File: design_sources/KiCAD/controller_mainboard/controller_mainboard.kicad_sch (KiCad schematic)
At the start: 34 parts, among them J1 XT-90, J10 01x08_2.54mm _socket, J11 2P_screw_term, J12 2P_screw_term, J13 2P_screw_term, J14 2P_screw_term, J2 XT-60, J24 XT-60, J25 XT-60, J3 USB_C_Receptacle_USB2.0_16P, J4 01x08_2.54mm _socket, J5 01x08_2.54mm _socket, J6 01x08_2.54mm _socket, J7 02x18_2.54mm_socket, J8 Conn_01x10_2.54mm_socket, J9 01x08_2.54mm _socket, Q1 2N7002, U12 USBLC6-4SC6

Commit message: Advanced the hardware layout further.
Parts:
- added H1, H2, H3, H4, H5, H6, H7, H8: MountingHole, MountingHole:MountingHole_3.2mm_M3_DIN965, symbol Mechanical:MountingHole
- J7: footprint Connector_PinHeader_2.54mm:PinHeader_2x18_P2.54mm_Vertical -> Connector_PinSocket_2.54mm:PinSocket_2x18_P2.54mm_Vertical

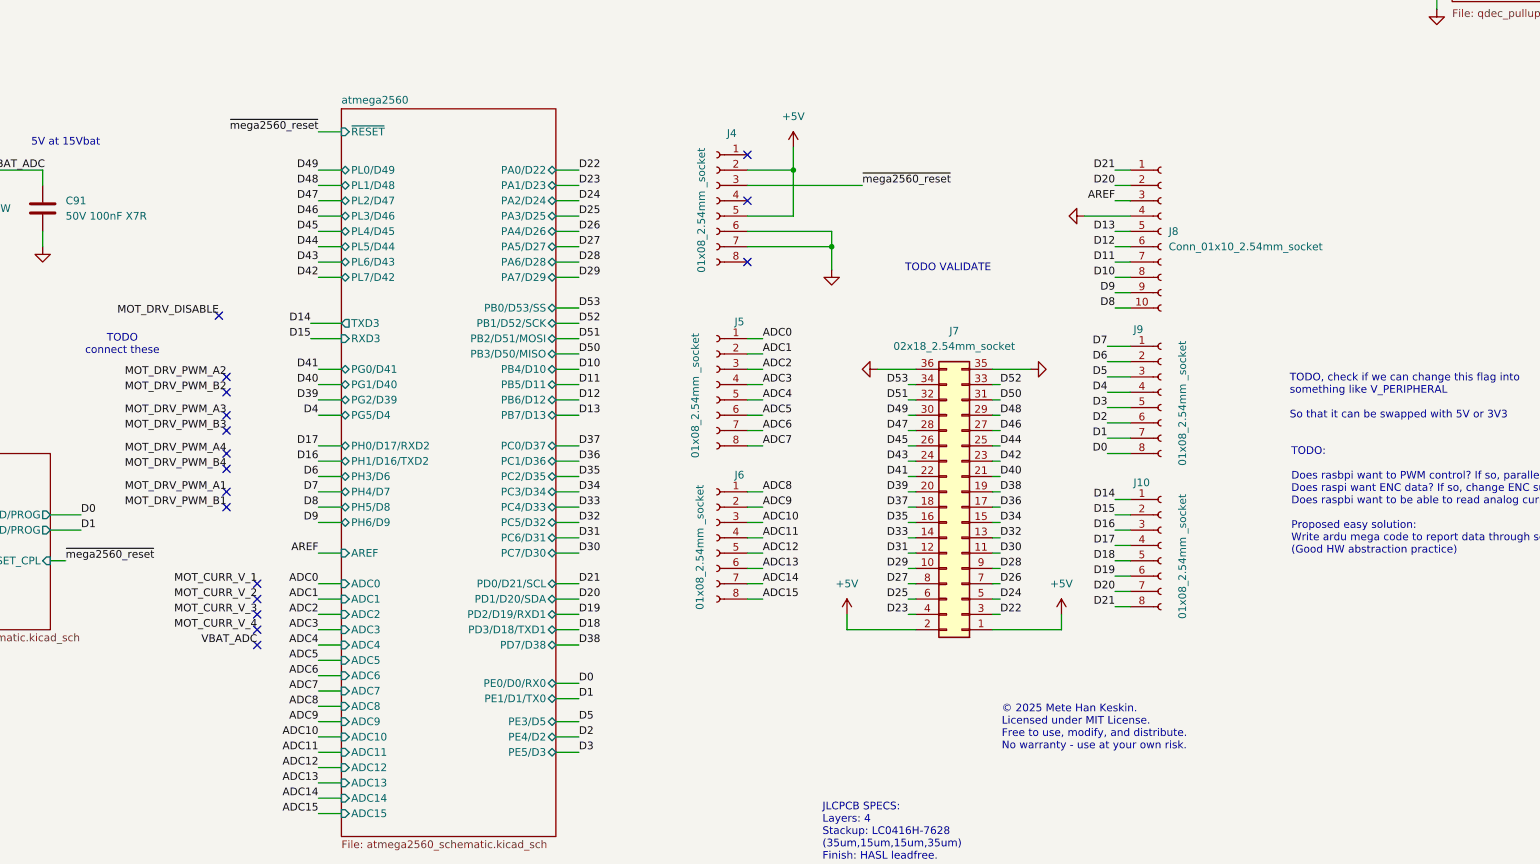
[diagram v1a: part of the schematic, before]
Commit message: Nearly finalized hardware layout. TODO add extra GND stitching vias, label IO numbers on silk, add cool silk drawings
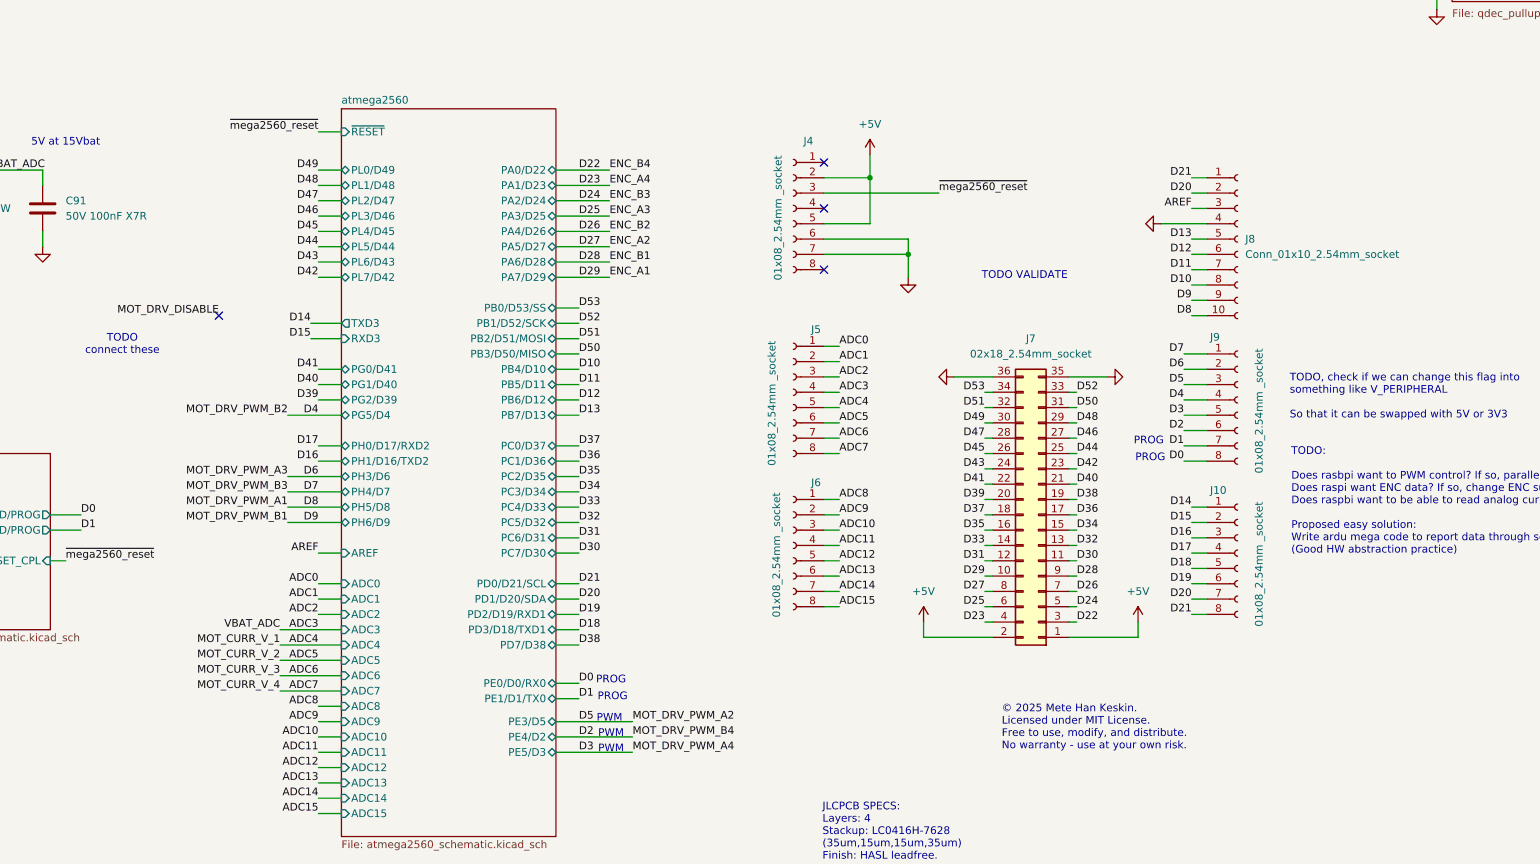
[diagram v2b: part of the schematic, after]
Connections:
- net VBAT_ADC is gone; now on net ADC3: C91.2, R80.2, R81.1
- no-connect marks 21 -> 8
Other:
- note added: "PROG"
- note added: "PWM"
- moved on the sheet: J10, J4, J5, J6, J7, J8, J9

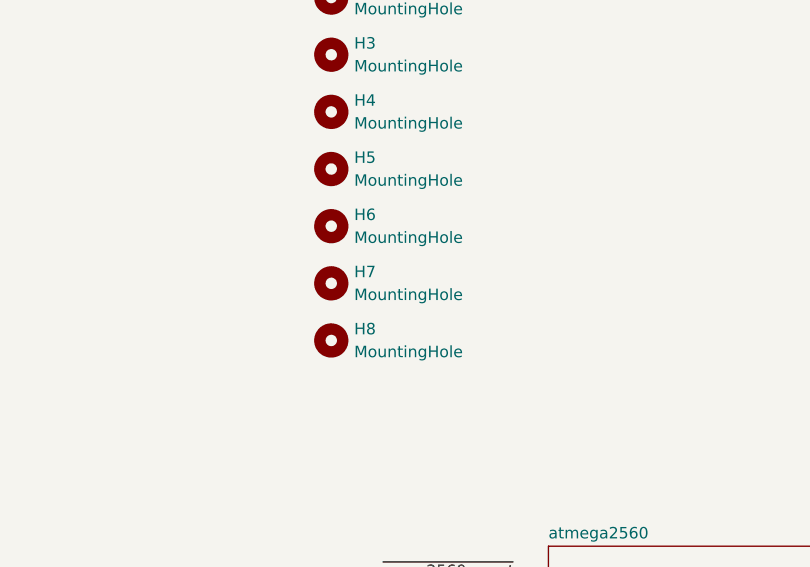
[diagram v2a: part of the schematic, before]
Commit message: Added via&silk naming job done, added PCBA renders
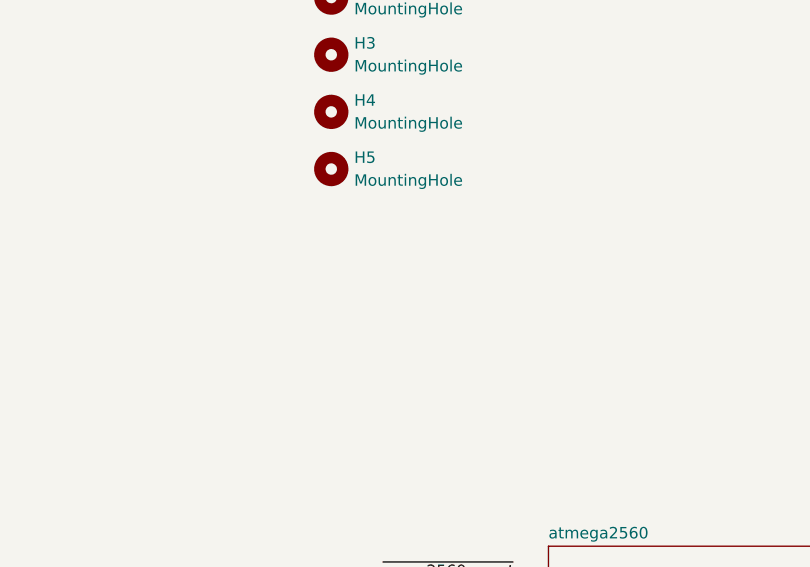
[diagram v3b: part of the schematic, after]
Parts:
- removed H6, H7, H8: MountingHole, MountingHole:MountingHole_3.2mm_M3_DIN965, symbol Mechanical:MountingHole
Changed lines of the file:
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@@
 	)
 	(symbol
-		(lib_id "Mechanical:MountingHole")
-		(at 166.37 110.49 0)
-		(unit 1)
-		(exclude_from_sim yes)
-		(in_bom no)
-		(on_board yes)
-		(dnp no)
-		(fields_autoplaced yes)
-		(property "Reference" "H6"
-			(at 168.91 109.2199 0)
-			(effects
-				(font
-					(size 1.27 1.27)
-				)
-				(justify left)
-			)
-		)
-		(property "Value" "MountingHole"
-			(at 168.91 111.7599 0)
-			(effects
-				(font
-					(size 1.27 1.27)
-				)
-				(justify left)
-			)
-		)
-		(property "Footprint" "MountingHole:MountingHole_3.2mm_M3_DIN965"
-			(at 166.37 110.49 0)
-			(effects
-				(font
-					(size 1.27 1.27)
-				)
-				(hide yes)
-			)
-		)
-		(property "Datasheet" "~"
-			(at 166.37 110.49 0)
-			(effects
-				(font
-					(size 1.27 1.27)
-				)
-				(hide yes)
-			)
-		)
-		(property "Description" "Mounting Hole without connection"
-			(at 166.37 110.49 0)
-			(effects
-				(font
-					(size 1.27 1.27)
-				)
-				(hide yes)
-			)
-		)
-		(instances
-			(project "controller_mainboard"
-				(path "/0fdfffec-3d24-4249-8ba9-dae7a6ccc250"
-					(reference "H6")
-					(unit 1)
-				)
-			)
-		)
-	)
-	(symbol
 		(lib_id "Device:R")
 		(at 87.63 158.75 0)
@@
 	)
 	(symbol
-		(lib_id "Mechanical:MountingHole")
-		(at 166.37 123.19 0)
-		(unit 1)
-		(exclude_from_sim yes)
-		(in_bom no)
-		(on_board yes)
-		(dnp no)
-		(fields_autoplaced yes)
-		(property "Reference" "H8"
-			(at 168.91 121.9199 0)
-			(effects
-				(font
-					(size 1.27 1.27)
-				)
-				(justify left)
-			)
-		)
-		(property "Value" "MountingHole"
-			(at 168.91 124.4599 0)
-			(effects
-				(font
-					(size 1.27 1.27)
-				)
-				(justify left)
-			)
-		)
-		(property "Footprint" "MountingHole:MountingHole_3.2mm_M3_DIN965"
-			(at 166.37 123.19 0)
-			(effects
-				(font
-					(size 1.27 1.27)
-				)
-				(hide yes)
-			)
-		)
-		(property "Datasheet" "~"
-			(at 166.37 123.19 0)
-			(effects
-				(font
-					(size 1.27 1.27)
-				)
-				(hide yes)
-			)
-		)
-		(property "Description" "Mounting Hole without connection"
-			(at 166.37 123.19 0)
-			(effects
-				(font
-					(size 1.27 1.27)
-				)
-				(hide yes)
-			)
-		)
-		(instances
-			(project "controller_mainboard"
-				(path "/0fdfffec-3d24-4249-8ba9-dae7a6ccc250"
-					(reference "H8")
-					(unit 1)
-				)
-			)
-		)
-	)
-	(symbol
 		(lib_id "power:GND")
 		(at 369.57 46.99 0)
@@
 					(unit 1)
 				)
-			)
-		)
-	)
-	(symbol
-		(lib_id "Mechanical:MountingHole")
-		(at 166.37 116.84 0)
-		(unit 1)
-		(exclude_from_sim yes)
-		(in_bom no)
-		(on_board yes)
-		(dnp no)
-		(fields_autoplaced yes)
-		(property "Reference" "H7"
-			(at 168.91 115.5699 0)
-			(effects
-				(font
-					(size 1.27 1.27)
-				)
-				(justify left)
-			)
-		)
-		(property "Value" "MountingHole"
-			(at 168.91 118.1099 0)
-			(effects
-				(font
-					(size 1.27 1.27)
-				)
-				(justify left)
-			)
-		)
-		(property "Footprint" "MountingHole:MountingHole_3.2mm_M3_DIN965"
-			(at 166.37 116.84 0)
-			(effects
-				(font
-					(size 1.27 1.27)
-				)
-				(hide yes)
-			)
-		)
-		(property "Datasheet" "~"
-			(at 166.37 116.84 0)
-			(effects
-				(font
-					(size 1.27 1.27)
-				)
-				(hide yes)
-			)
-		)
-		(property "Description" "Mounting Hole without connection"
-			(at 166.37 116.84 0)
-			(effects
-				(font
-					(size 1.27 1.27)
-				)
-				(hide yes)
-			)
-		)
-		(instances
-			(project "controller_mainboard"
-				(path "/0fdfffec-3d24-4249-8ba9-dae7a6ccc250"
-					(reference "H7")
-					(unit 1)
-				)

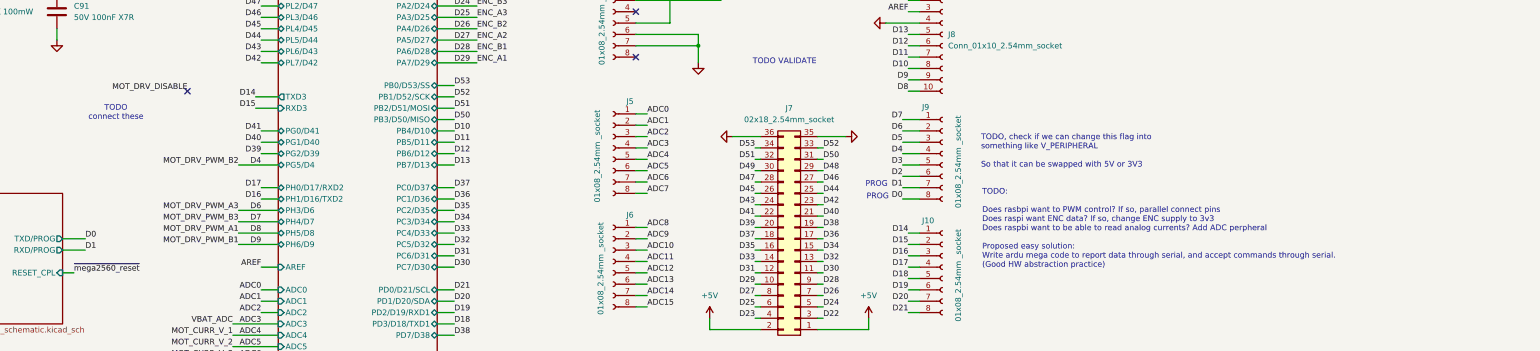
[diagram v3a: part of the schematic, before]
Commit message: Re-checked DRC, differing footprint warnings are fine, added production files for JLC placement and prod. TODO, maybe cool silk art at the bottom and definitive order list.
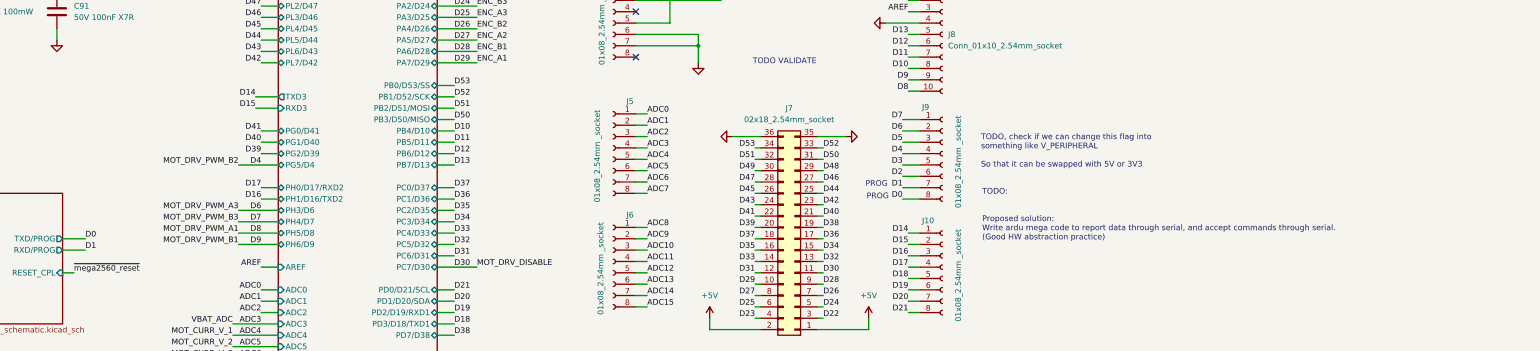
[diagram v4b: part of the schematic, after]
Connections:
- no-connect marks 8 -> 7
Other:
- note added: "TODO: Proposed solution: Write ardu mega code to report data through serial, and accept commands through serial. (Good HW abstraction practice)"
- note removed: "TODO connect these"
- note removed: "TODO: Does rasbpi want to PWM control? If so, parallel connect pins Does raspi want ENC data? If so, change ENC supply to 3v3 Does raspbi want to be able to read analog currents? Add ADC perpheral Proposed easy solution: Write ardu mega code to report data through serial, and accept commands through serial. (Good HW abstraction practice)"
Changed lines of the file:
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@@
 		)
 	)
-	(text "TODO: \n\nDoes rasbpi want to PWM control? If so, parallel connect pins\nDoes raspi want ENC data? If so, change ENC supply to 3v3\nDoes raspbi want to be able to read analog currents? Add ADC perpheral\n\nProposed easy solution:\nWrite ardu mega code to report data through serial, and accept commands through serial.\n(Good HW abstraction practice)"
+	(text "TODO: \n\n\nProposed solution:\nWrite ardu mega code to report data through serial, and accept commands through serial.\n(Good HW abstraction practice)"
 		(exclude_from_sim no)
 		(at 347.98 202.184 0)
@@
 		)
 	)
-	(text "TODO\nconnect these"
-		(exclude_from_sim no)
-		(at 154.178 185.166 0)
-		(effects
-			(font
-				(size 1.27 1.27)
-			)
-		)
-	)
 	(text "PERFECT!!!\n\nUSBLC6-4SC6-ES  C5180279\n\nSEUC10F5V4U C5126804\n\nIP4220CZ6-ES C5199235\n\n\n\n"
 		(exclude_from_sim no)
@@
 	)
 	(no_connect
-		(at 170.18 180.34)
-	)
-	(no_connect
 		(at 270.51 154.94)
 	)
@@
 	(wire
 		(pts
-			(xy 229.87 219.71) (xy 226.06 219.71)
+			(xy 226.06 219.71) (xy 234.95 219.71)
 		)
 		(stroke
@@
 	)
 	(label "MOT_DRV_DISABLE"
-		(at 170.18 180.34 180)
+		(at 234.95 219.71 0)
 		(effects
 			(font
 				(size 1.27 1.27)
 			)
-			(justify right bottom)
+			(justify left bottom)
 		)
 	)

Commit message: Changed JLCPCB field to LCSC
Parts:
- C91: JLCPCB C14663 -> (none); LCSC (none) -> C14663
- D1: JLCPCB C2286 -> (none); LCSC (none) -> C2286
- D2: JLCPCB C22452 -> (none); LCSC (none) -> C22452
- D36: JLCPCB C2297 -> (none); LCSC (none) -> C2297
- FB1: JLCPCB C1015 -> (none); LCSC (none) -> C1015
- J3: JLCPCB C2927038 -> (none); LCSC (none) -> C2927038
- Q1: JLCPCB C8545 -> (none); LCSC (none) -> C8545
- R1, R81: JLCPCB C25744 -> (none); LCSC (none) -> C25744
- R4, R62, R63: JLCPCB C11702 -> (none); LCSC (none) -> C11702
- R5, R6, R80: JLCPCB C23186 -> (none); LCSC (none) -> C23186
- R7, R8: JLCPCB C23345 -> (none); LCSC (none) -> C23345
- U12: JLCPCB C5180279 -> (none); LCSC (none) -> C5180279
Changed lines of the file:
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@@
 			)
 		)
-		(property "JLCPCB" "C23186"
+		(property "LCSC" "C23186"
 			(at 121.92 161.29 0)
 			(effects
@@
 			)
 		)
-		(property "JLCPCB" "C25744"
+		(property "LCSC" "C25744"
 			(at 34.29 123.19 0)
 			(effects
@@
 			)
 		)
-		(property "JLCPCB" "C2297"
-			(at 90.17 168.91 0)
+		(property "LCSC" "C2297"
+			(at 90.17 168.91 90)
 			(effects
 				(font
@@
 			)
 		)
-		(property "JLCPCB" "C25744"
+		(property "LCSC" "C25744"
 			(at 121.92 151.13 0)
 			(effects
@@
 			)
 		)
-		(property "JLCPCB" "C23186"
-			(at 80.01 205.74 0)
+		(property "LCSC" "C23186"
+			(at 80.01 205.74 90)
 			(effects
 				(font
@@
 			)
 		)
-		(property "JLCPCB" "C1015"
+		(property "LCSC" "C1015"
 			(at 38.1 247.65 90)
 			(effects
@@
 			)
 		)
-		(property "JLCPCB" "C11702"
+		(property "LCSC" "C11702"
 			(at 87.63 158.75 0)
 			(effects
@@
 			)
 		)
-		(property "JLCPCB" "C23345"
-			(at 95.25 214.63 0)
+		(property "LCSC" "C23345"
+			(at 95.25 214.63 90)
 			(effects
 				(font
@@
 			)
 		)
-		(property "JLCPCB" "C5180279"
+		(property "LCSC" "C5180279"
 			(at 87.63 257.81 0)
 			(effects
@@
 			)
 		)
-		(property "JLCPCB" "C23345"
-			(at 95.25 217.17 0)
+		(property "LCSC" "C23345"
+			(at 95.25 217.17 90)
 			(effects
 				(font
@@
 			)
 		)
-		(property "JLCPCB" "C2286"
+		(property "LCSC" "C2286"
 			(at 57.15 55.88 0)
 			(effects
@@
 			)
 		)
-		(property "JLCPCB" "C11702"
+		(property "LCSC" "C11702"
 			(at 90.17 158.75 0)
 			(effects
@@
 			)
 		)
-		(property "JLCPCB" "C14663"
+		(property "LCSC" "C14663"
 			(at 140.97 162.56 0)
 			(effects
@@
 			)
 		)
-		(property "JLCPCB" "C11702"
-			(at 48.26 55.88 0)
+		(property "LCSC" "C11702"
+			(at 48.26 55.88 90)
 			(effects
 				(font
@@
 			)
 		)
-		(property "JLCPCB" "C8545"
+		(property "LCSC" "C8545"
 			(at 40.64 118.11 0)
 			(effects
@@
 			)
 		)
-		(property "JLCPCB" "C2927038"
+		(property "LCSC" "C2927038"
 			(at 36.83 213.36 0)
 			(effects
@@
 			)
 		)
-		(property "JLCPCB" "C22452"
-			(at 115.57 193.04 90)
+		(property "LCSC" "C22452"
+			(at 115.57 193.04 0)
 			(effects
 				(font
@@
 			)
 		)
-		(property "JLCPCB" "C23186"
-			(at 80.01 203.2 0)
+		(property "LCSC" "C23186"
+			(at 80.01 203.2 90)
 			(effects
 				(font
